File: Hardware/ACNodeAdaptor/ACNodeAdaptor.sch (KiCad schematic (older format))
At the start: 6 parts, among them J1 Conn_01x02, J2 Conn_01x04_Male, J3 RJ45, U1 ISL8489EIBZ

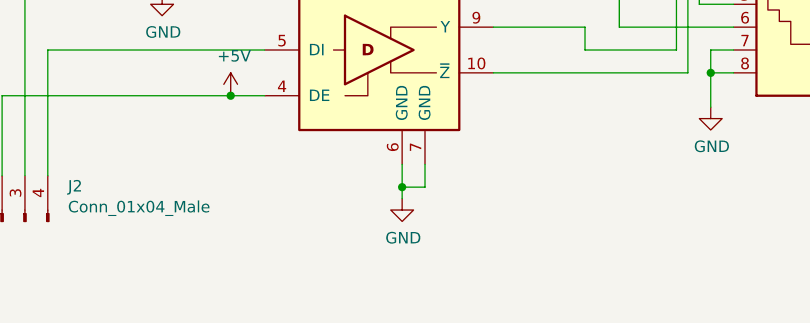
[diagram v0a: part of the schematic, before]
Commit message: Note about 3.3V operation (e.g with a launchpad)
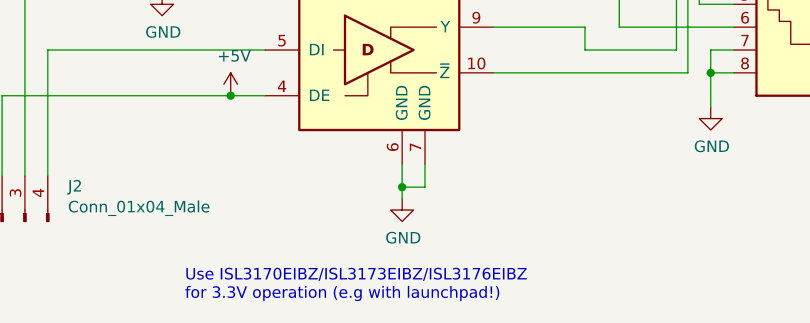
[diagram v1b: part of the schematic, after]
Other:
- note added: "Use ISL3170EIBZ/ISL3173EIBZ/ISL3176EIBZ\nfor 3.3V operation (e.g with launchpad!)"
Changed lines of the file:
@@
 Wire Wire Line
 	4000 3100 4950 3100
+Text Notes 4600 4200 0    50   ~ 0
+Use ISL3170EIBZ/ISL3173EIBZ/ISL3176EIBZ\nfor 3.3V operation (e.g with launchpad!)
 $EndSCHEMATC
